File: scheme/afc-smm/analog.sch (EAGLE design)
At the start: 11 parts, among them IC1 OP1177R, IC10 LM2931-5.0, IC2 TL082D, IC3 AD8515RJ, IC4 AD8615RJ, IC5 AD8221R, IC6 AD7476, IC7 REF3033, IC8 LM337LM, IC9 317EMP

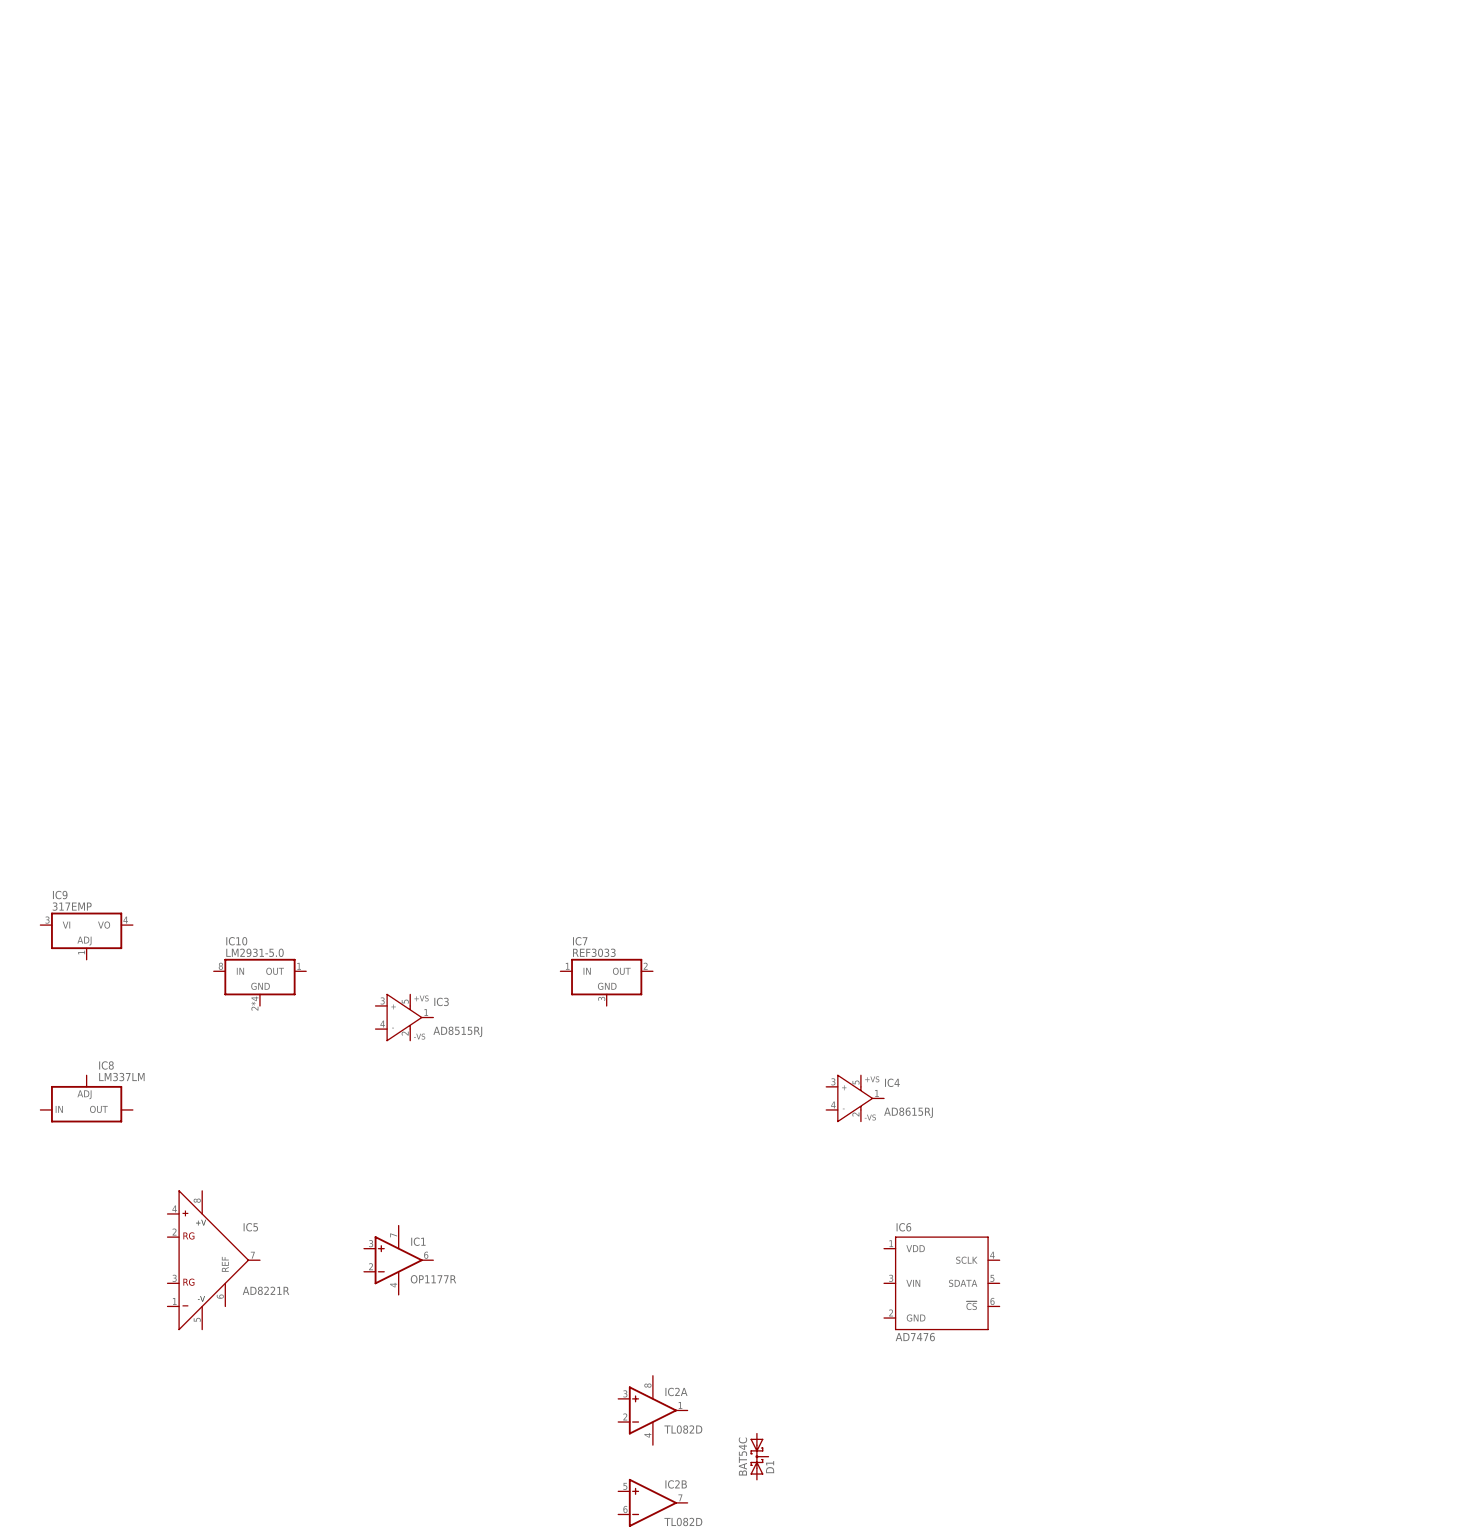
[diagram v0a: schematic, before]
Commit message: add some element on schematic, begin connecting
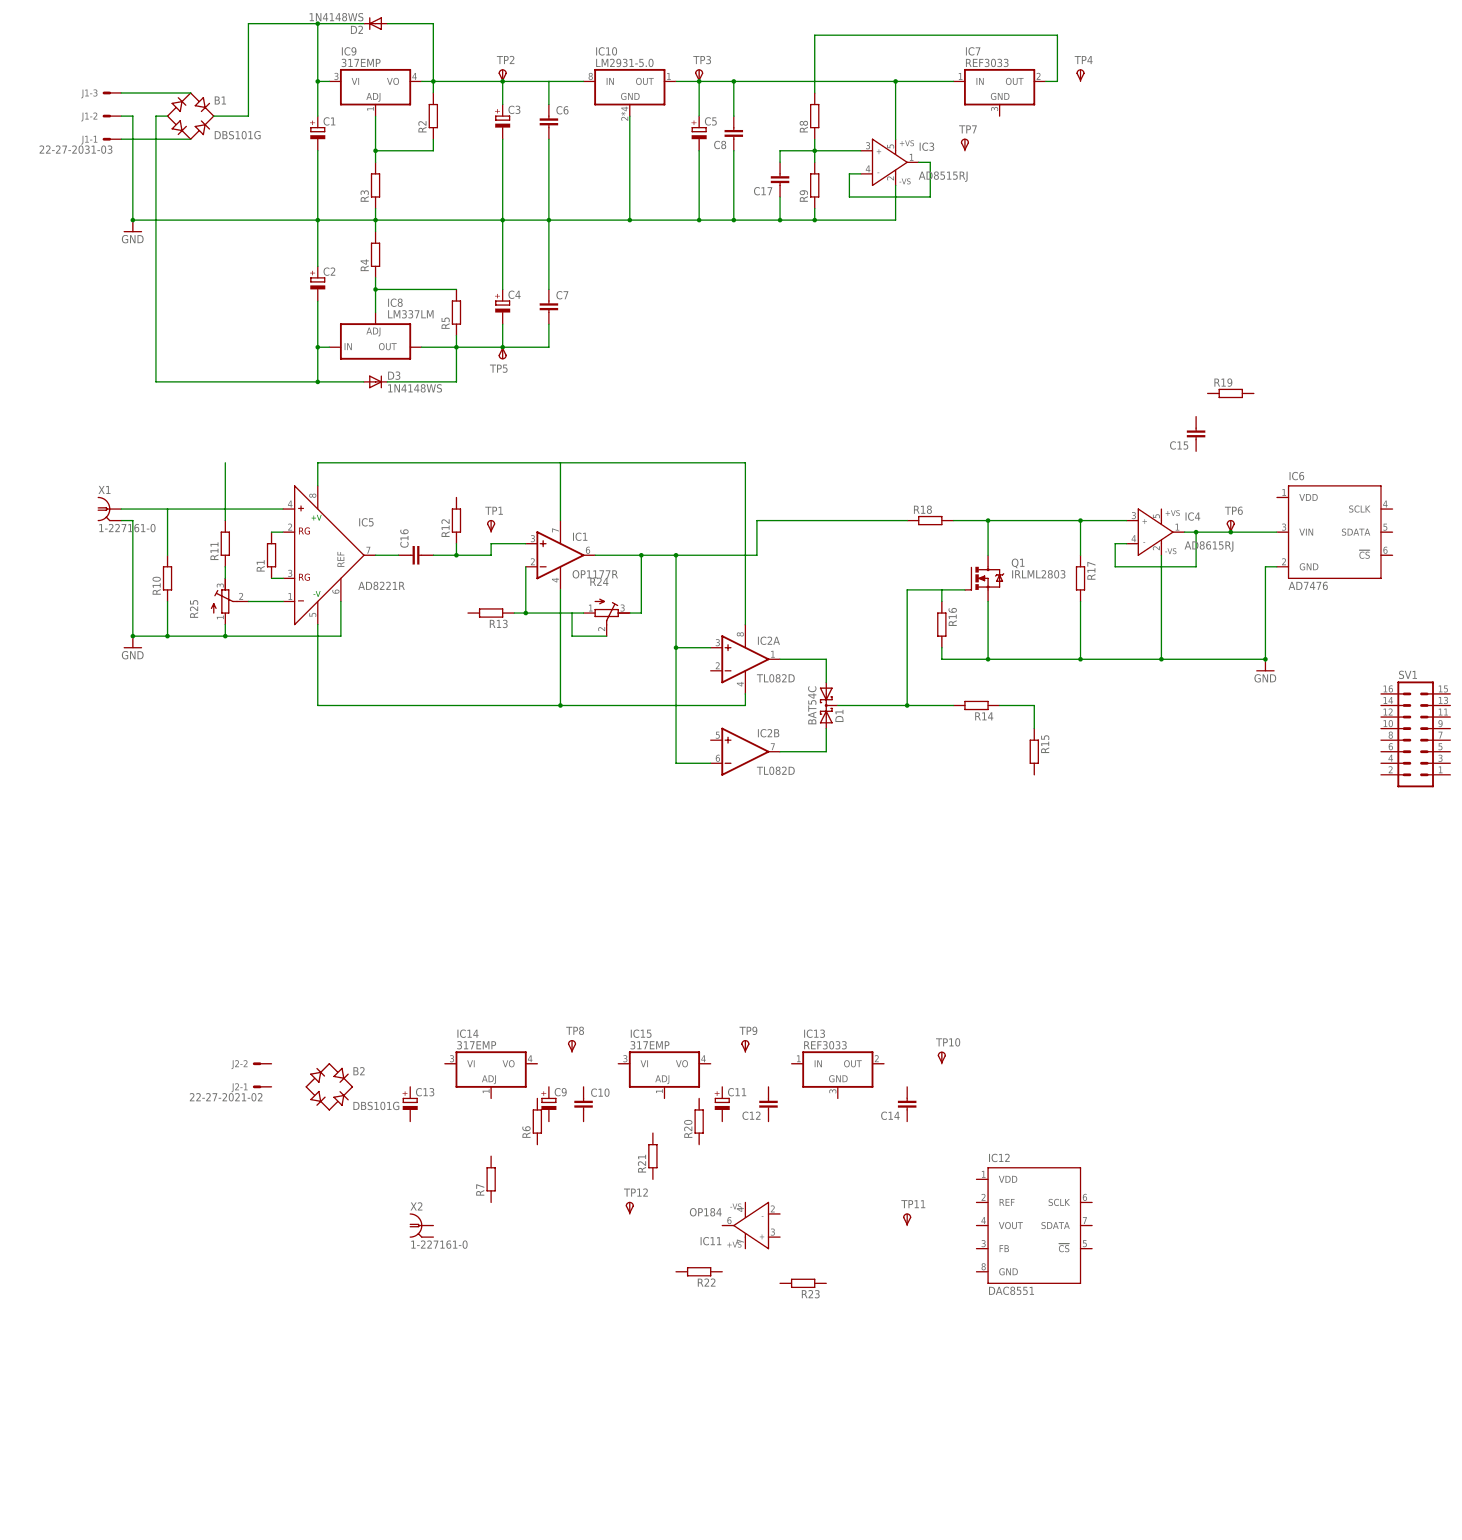
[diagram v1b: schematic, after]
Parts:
- added B1, B2: DBS101G, rectifier:DBS101G
- added C1, C13, C2: (no value), rcl:CPOL-EUE3.5-8
- added C10, C6, C7: (no value), rcl:C-EUC0805K
- added C11, C5: (no value), rcl:CPOL-EUE2.5-5
- added C12, C14, C15, C16, C17, C8: (no value), rcl:C-EUC0603
- added C3, C4, C9: (no value), rcl:CPOL-EUE2.5-6
- added D2, D3: 1N4148WS, afc-smm:1N4148WS
- added IC11: OP184, afc-smm:OP184
- added IC12: DAC8551, afc-smm:DAC8551
- added IC13: REF3033, afc-smm:REF3033
- added IC14, IC15: 317EMP, linear:317EMP
- added J1: 22-27-2031-03, con-molex:22-27-2031-03
- added J2: 22-27-2021-02, con-molex:22-27-2021-02
- added Q1: IRLML2803, afc-smm:IRLML2803
- added R1, R2, R3, R4, R5, R6, R7: (no value), rcl:R-EU_R0805
- added R10, R11, R12, R13, R14, R15, R16, R17, R18, R19, R20, R21, R22, R23, R8, R9: (no value), rcl:R-EU_R0603
- added R24, R25: (no value), rcl:R-TRIMM3296W
- added SV1: (no value), con-lstb:MA08-2W
- added TP1, TP10, TP11, TP12, TP2, TP3, TP4, TP5, TP6, TP7, TP8, TP9: TPSB2,54, testpad:TPSB2,54
- added X1, X2: 1-227161-0, con-coax:1-227161-0
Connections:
- new net GND: C1.-, C17.1, C2.+, C3.-, C4.+, C5.-, C6.2, C7.1, C8.1, IC10.GND, IC3.-VS, IC4.-VS, IC5.REF, IC6.GND, J1-2.S, Q1.S, R10.1, R16.2, R17.2, R25.A, R3.1, R4.2, R9.1, X1.2
- new net N$1: IC4.IN-, IC4.OUT, IC6.VIN, TP6.PP
- new net N$10: IC5.RG@1, R1.2
- new net N$11: IC5.RG@2, R1.1
- new net N$12: C16.1, IC5.OUT
- new net N$13: R24.S
- new net N$14: IC1.-IN, R13.1, R24.A
- new net N$15: C16.2, IC1.+IN, R12.1
- new net N$17: IC5.-, R25.S
- new net N$18: R11.1, R25.E
- new net N$19: IC5.+, R10.2, X1.1
- new net N$2: IC4.IN+, Q1.D, R17.1, R18.2
- new net N$20: R11.2
- new net N$21: B1.+, C1.+, D2.C, IC9.VI
- new net N$22: C4.-, C7.2, D3.C, IC8.OUT, R5.1, TP5.PP
- new net N$23: C3.+, C6.1, D2.A, IC10.IN, IC9.VO, R2.2, TP2.PP
- new net N$24: IC8.ADJ, R4.1, R5.2
- new net N$25: IC9.ADJ, R2.1, R3.2
- new net N$28: C5.+, C8.2, IC10.OUT, IC3.+VS, IC7.IN, TP3.PP
- new net N$29: IC3.IN-, IC3.OUT
- new net N$30: C17.2, IC3.IN+, R8.1, R9.2
- new net N$31: IC1.V+, IC2P.V+, IC5.+V
- new net N$32: IC7.OUT, R8.2
- new net N$34: B1.-, C2.-, D3.A, IC8.IN
- new net N$35: B1.AC1, J1-3.S
- new net N$36: B1.AC2, J1-1.S
- new net N$4: D1.A1, IC2A.OUT
- new net N$5: D1.CC, Q1.G, R14.2, R16.1
- new net N$6: D1.A2, IC2B.OUT
- new net N$7: IC1.V-, IC2P.V-, IC5.-V
- new net N$8: R14.1, R15.1
- new net N$9: IC1.OUT, IC2A.+IN, IC2B.-IN, R18.1, R24.E
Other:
- moved on the sheet: D1, IC1, IC10, IC2A, IC2B, IC3, IC4, IC5, IC6, IC7, IC8, IC9

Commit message: start to make raw PCB
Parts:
- added LED1, LED2: (no value), led:LEDCHIPLED_0805
- added R26, R27: (no value), rcl:R-EU_R0603
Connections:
- net N$28 renamed +5V
- removed net N$22: C4.-, C7.2, D3.C, IC8.OUT, R5.1, TP5.PP
- removed net N$23: C3.+, C6.1, D2.A, IC10.IN, IC9.VO, R2.2, TP2.PP
- removed net N$31: IC1.V+, IC2P.V+, IC5.+V
- removed net N$32: IC7.OUT, R8.2
- removed net N$7: IC1.V-, IC2P.V-, IC5.-V
- new net +12V: C3.+, C6.1, D2.A, IC1.V+, IC10.IN, IC2P.V+, IC5.+V, IC9.VO, R2.2, TP2.PP
- new net +3.3V: IC6.VDD, IC7.OUT, R8.2, TP4.PP
- new net -12V: C4.-, C7.2, D3.C, IC1.V-, IC2P.V-, IC5.-V, IC8.OUT, R5.1, TP5.PP
- new net N$27: C15.2, IC2A.-IN, IC4.+VS, R19.1
- net GND: now also IC2B.+IN, IC7.GND, R15.2
- net N$15: now also TP1.PP
- net N$29: now also R12.2, R13.2, TP7.PP
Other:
- moved on the sheet: IC1, IC11, R13, R24, TP1, TP7

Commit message: commit before vocation
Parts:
- removed C15: (no value), rcl:C-EUC0603
- added C18, C19: (no value), rcl:CPOL-EUSMCA
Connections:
- removed net N$14: IC1.-IN, R13.1, R24.A
- net +3.3V: now also C18.+, R19.2
- net GND: now also C18.-, C19.-
- net N$13: now also IC1.-IN, R13.1, R24.A
- net N$27: now also C19.+; no longer C15.2
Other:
- moved on the sheet: LED1, LED2, R19, R26, R27, SV1
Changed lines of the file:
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@@
 <part name="C16" library="rcl" deviceset="C-EU" device="C0603"/>
 <part name="C8" library="rcl" deviceset="C-EU" device="C0603"/>
-<part name="C15" library="rcl" deviceset="C-EU" device="C0603"/>
 <part name="C12" library="rcl" deviceset="C-EU" device="C0603"/>
 <part name="C14" library="rcl" deviceset="C-EU" device="C0603"/>
@@
 <part name="GND4" library="supply1" deviceset="GND" device=""/>
 <part name="GND5" library="supply1" deviceset="GND" device=""/>
+<part name="C18" library="rcl" deviceset="CPOL-EU" device="SMCA"/>
+<part name="C19" library="rcl" deviceset="CPOL-EU" device="SMCA"/>
 </parts>
 <sheets>
@@
 <instance part="TP11" gate="G$1" x="175.26" y="63.5"/>
 <instance part="TP12" gate="G$1" x="114.3" y="66.04"/>
-<instance part="SV1" gate="1" x="287.02" y="167.64"/>
+<instance part="SV1" gate="1" x="320.04" y="142.24"/>
 <instance part="C9" gate="G$1" x="96.52" y="88.9"/>
 <instance part="C10" gate="G$1" x="104.14" y="88.9"/>
@@
 <instance part="R17" gate="G$1" x="213.36" y="203.2" rot="R270"/>
 <instance part="R18" gate="G$1" x="180.34" y="215.9"/>
-<instance part="R19" gate="G$1" x="246.38" y="243.84"/>
+<instance part="R19" gate="G$1" x="248.92" y="220.98"/>
 <instance part="R20" gate="G$1" x="129.54" y="83.82" rot="R90"/>
 <instance part="R21" gate="G$1" x="119.38" y="76.2" rot="R90"/>
@@
 <instance part="C16" gate="G$1" x="66.04" y="208.28" rot="R90"/>
 <instance part="C8" gate="G$1" x="137.16" y="299.72" rot="R180"/>
-<instance part="C15" gate="G$1" x="238.76" y="233.68" rot="R180"/>
 <instance part="C12" gate="G$1" x="144.78" y="86.36" rot="R180"/>
 <instance part="C14" gate="G$1" x="175.26" y="86.36" rot="R180"/>
@@
 <instance part="GND2" gate="1" x="5.08" y="187.96"/>
 <instance part="GND3" gate="1" x="254" y="182.88"/>
-<instance part="LED1" gate="G$1" x="309.88" y="175.26"/>
-<instance part="LED2" gate="G$1" x="322.58" y="175.26"/>
-<instance part="R26" gate="G$1" x="309.88" y="187.96" rot="R270"/>
-<instance part="R27" gate="G$1" x="322.58" y="187.96" rot="R270"/>
+<instance part="LED1" gate="G$1" x="335.28" y="210.82"/>
+<instance part="LED2" gate="G$1" x="342.9" y="210.82"/>
+<instance part="R26" gate="G$1" x="335.28" y="223.52" rot="R270"/>
+<instance part="R27" gate="G$1" x="342.9" y="223.52" rot="R270"/>
 <instance part="GND4" gate="1" x="129.54" y="152.4"/>
 <instance part="GND5" gate="1" x="203.2" y="149.86"/>
+<instance part="C18" gate="G$1" x="208.28" y="307.34"/>
+<instance part="C19" gate="G$1" x="241.3" y="198.12"/>
 </instances>
 <busses>
@@
 <wire x1="109.22" y1="187.96" x2="101.6" y2="187.96" width="0.1524" layer="91"/>
 <wire x1="101.6" y1="187.96" x2="101.6" y2="193.04" width="0.1524" layer="91"/>
-</segment>
-</net>
-<net name="N$14" class="0">
-<segment>
 <pinref part="R24" gate="G$1" pin="A"/>
 <pinref part="R13" gate="G$1" pin="1"/>
-<wire x1="104.14" y1="193.04" x2="91.44" y2="193.04" width="0.1524" layer="91"/>
+<wire x1="104.14" y1="193.04" x2="101.6" y2="193.04" width="0.1524" layer="91"/>
 <pinref part="IC1" gate="G$1" pin="-IN"/>
+<wire x1="101.6" y1="193.04" x2="91.44" y2="193.04" width="0.1524" layer="91"/>
 <wire x1="91.44" y1="193.04" x2="88.9" y2="193.04" width="0.1524" layer="91"/>
 <wire x1="91.44" y1="203.2" x2="91.44" y2="193.04" width="0.1524" layer="91"/>
 <junction x="91.44" y="193.04"/>
+<junction x="101.6" y="193.04"/>
 </segment>
 </net>
@@
 <pinref part="IC7" gate="G$1" pin="OUT"/>
 <wire x1="208.28" y1="312.42" x2="205.74" y2="312.42" width="0.1524" layer="91"/>
-<pinref part="IC6" gate="G$1" pin="VDD"/>
-<wire x1="256.54" y1="220.98" x2="251.46" y2="220.98" width="0.1524" layer="91"/>
-<wire x1="251.46" y1="220.98" x2="251.46" y2="312.42" width="0.1524" layer="91"/>
-<wire x1="251.46" y1="312.42" x2="213.36" y2="312.42" width="0.1524" layer="91"/>
+<wire x1="254" y1="220.98" x2="254" y2="312.42" width="0.1524" layer="91"/>
+<wire x1="254" y1="312.42" x2="213.36" y2="312.42" width="0.1524" layer="91"/>
 <pinref part="TP4" gate="G$1" pin="PP"/>
 <wire x1="213.36" y1="312.42" x2="208.28" y2="312.42" width="0.1524" layer="91"/>
 <junction x="213.36" y="312.42"/>
+<pinref part="C18" gate="G$1" pin="+"/>
+<wire x1="208.28" y1="309.88" x2="208.28" y2="312.42" width="0.1524" layer="91"/>
+<pinref part="IC6" gate="G$1" pin="VDD"/>
+<wire x1="256.54" y1="220.98" x2="254" y2="220.98" width="0.1524" layer="91"/>
+<pinref part="R19" gate="G$1" pin="2"/>
+<junction x="254" y="220.98"/>
+<junction x="208.28" y="312.42"/>
 </segment>
 </net>
@@
 <wire x1="195.58" y1="304.8" x2="195.58" y2="281.94" width="0.1524" layer="91"/>
 <wire x1="195.58" y1="281.94" x2="172.72" y2="281.94" width="0.1524" layer="91"/>
+<pinref part="C18" gate="G$1" pin="-"/>
+<wire x1="208.28" y1="302.26" x2="208.28" y2="281.94" width="0.1524" layer="91"/>
+<wire x1="208.28" y1="281.94" x2="195.58" y2="281.94" width="0.1524" layer="91"/>
+<junction x="195.58" y="281.94"/>
 </segment>
 <segment>
@@
 <wire x1="256.54" y1="205.74" x2="254" y2="205.74" width="0.1524" layer="91"/>
 <wire x1="254" y1="205.74" x2="254" y2="185.42" width="0.1524" layer="91"/>
-<wire x1="254" y1="185.42" x2="231.14" y2="185.42" width="0.1524" layer="91"/>
+<wire x1="254" y1="185.42" x2="241.3" y2="185.42" width="0.1524" layer="91"/>
 <pinref part="GND3" gate="1" pin="GND"/>
 <junction x="254" y="185.42"/>
 <junction x="213.36" y="185.42"/>
 <junction x="231.14" y="185.42"/>
+<pinref part="C19" gate="G$1" pin="-"/>
+<wire x1="241.3" y1="185.42" x2="231.14" y2="185.42" width="0.1524" layer="91"/>
+<wire x1="241.3" y1="193.04" x2="241.3" y2="185.42" width="0.1524" layer="91"/>
+<junction x="241.3" y="185.42"/>
 </segment>
 <segment>
@@
 <segment>
 <pinref part="R19" gate="G$1" pin="1"/>
-<pinref part="C15" gate="G$1" pin="2"/>
-<wire x1="241.3" y1="243.84" x2="238.76" y2="243.84" width="0.1524" layer="91"/>
-<wire x1="238.76" y1="243.84" x2="238.76" y2="238.76" width="0.1524" layer="91"/>
 <pinref part="IC4" gate="G$1" pin="+VS"/>
-<wire x1="231.14" y1="218.44" x2="231.14" y2="223.52" width="0.1524" layer="91"/>
-<wire x1="231.14" y1="223.52" x2="231.14" y2="243.84" width="0.1524" layer="91"/>
-<wire x1="231.14" y1="243.84" x2="238.76" y2="243.84" width="0.1524" layer="91"/>
+<wire x1="231.14" y1="218.44" x2="231.14" y2="220.98" width="0.1524" layer="91"/>
+<wire x1="231.14" y1="220.98" x2="241.3" y2="220.98" width="0.1524" layer="91"/>
 <pinref part="IC2" gate="A" pin="-IN"/>
+<wire x1="241.3" y1="220.98" x2="243.84" y2="220.98" width="0.1524" layer="91"/>
 <wire x1="132.08" y1="182.88" x2="129.54" y2="182.88" width="0.1524" layer="91"/>
-<wire x1="129.54" y1="182.88" x2="129.54" y2="223.52" width="0.1524" layer="91"/>
-<wire x1="129.54" y1="223.52" x2="231.14" y2="223.52" width="0.1524" layer="91"/>
-</segment>
-</net>
+<wire x1="129.54" y1="182.88" x2="129.54" y2="220.98" width="0.1524" layer="91"/>
+<wire x1="129.54" y1="220.98" x2="231.14" y2="220.98" width="0.1524" layer="91"/>
+<pinref part="C19" gate="G$1" pin="+"/>
+<wire x1="241.3" y1="200.66" x2="241.3" y2="220.98" width="0.1524" layer="91"/>
+<junction x="241.3" y="220.98"/>
+<junction x="231.14" y="220.98"/>
+</segment>
+</net>

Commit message: make analog in, not compleate yet
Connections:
- new net N$16: LED1.A, R26.2
- net GND: now also LED1.C, LED2.C
- net N$20: now also LED2.A, R27.2; no longer R11.2
- net N$29: now also R11.2
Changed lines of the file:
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@@
 <part name="C18" library="rcl" deviceset="CPOL-EU" device="SMCA"/>
 <part name="C19" library="rcl" deviceset="CPOL-EU" device="SMCA"/>
+<part name="GND6" library="supply1" deviceset="GND" device=""/>
 </parts>
 <sheets>
@@
 <instance part="C18" gate="G$1" x="208.28" y="307.34"/>
 <instance part="C19" gate="G$1" x="241.3" y="198.12"/>
+<instance part="GND6" gate="1" x="335.28" y="195.58"/>
 </instances>
 <busses>
@@
 </segment>
 </net>
-<net name="N$20" class="0">
-<segment>
-<pinref part="R11" gate="G$1" pin="2"/>
-<wire x1="25.4" y1="215.9" x2="25.4" y2="228.6" width="0.1524" layer="91"/>
-</segment>
-</net>
 <net name="+12V" class="0">
 <segment>
@@
 <pinref part="TP7" gate="G$1" pin="PP"/>
 <junction x="180.34" y="287.02"/>
+<pinref part="R11" gate="G$1" pin="2"/>
+<wire x1="25.4" y1="215.9" x2="25.4" y2="233.68" width="0.1524" layer="91"/>
+<wire x1="81.28" y1="233.68" x2="25.4" y2="233.68" width="0.1524" layer="91"/>
 </segment>
 </net>
@@
 <wire x1="203.2" y1="152.4" x2="203.2" y2="160.02" width="0.1524" layer="91"/>
 </segment>
+<segment>
+<pinref part="LED1" gate="G$1" pin="C"/>
+<pinref part="GND6" gate="1" pin="GND"/>
+<wire x1="335.28" y1="205.74" x2="335.28" y2="200.66" width="0.1524" layer="91"/>
+<pinref part="LED2" gate="G$1" pin="C"/>
+<wire x1="335.28" y1="200.66" x2="335.28" y2="198.12" width="0.1524" layer="91"/>
+<wire x1="342.9" y1="205.74" x2="342.9" y2="200.66" width="0.1524" layer="91"/>
+<wire x1="342.9" y1="200.66" x2="335.28" y2="200.66" width="0.1524" layer="91"/>
+<junction x="335.28" y="200.66"/>
+</segment>
 </net>
 <net name="N$38" class="0">
@@
 <wire x1="45.72" y1="312.42" x2="45.72" y2="325.12" width="0.1524" layer="91"/>
 <wire x1="45.72" y1="325.12" x2="55.88" y2="325.12" width="0.1524" layer="91"/>
+<junction x="45.72" y="312.42"/>
 </segment>
 </net>
@@
 <wire x1="55.88" y1="246.38" x2="45.72" y2="246.38" width="0.1524" layer="91"/>
 <wire x1="45.72" y1="246.38" x2="45.72" y2="254" width="0.1524" layer="91"/>
+<junction x="45.72" y="254"/>
 </segment>
 </net>
@@
 </segment>
 </net>
+<net name="N$16" class="0">
+<segment>
+<pinref part="LED1" gate="G$1" pin="A"/>
+<pinref part="R26" gate="G$1" pin="2"/>
+<wire x1="335.28" y1="213.36" x2="335.28" y2="218.44" width="0.1524" layer="91"/>
+</segment>
+</net>
+<net name="N$20" class="0">
+<segment>
+<pinref part="LED2" gate="G$1" pin="A"/>
+<pinref part="R27" gate="G$1" pin="2"/>
+<wire x1="342.9" y1="213.36" x2="342.9" y2="218.44" width="0.1524" layer="91"/>
+</segment>
+</net>
